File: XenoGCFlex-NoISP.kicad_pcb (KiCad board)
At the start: 2 copper layers, 23.6 x 20 mm, 21 parts, among them J1 AVR-ISP-6, U1 ATmega8A-AU

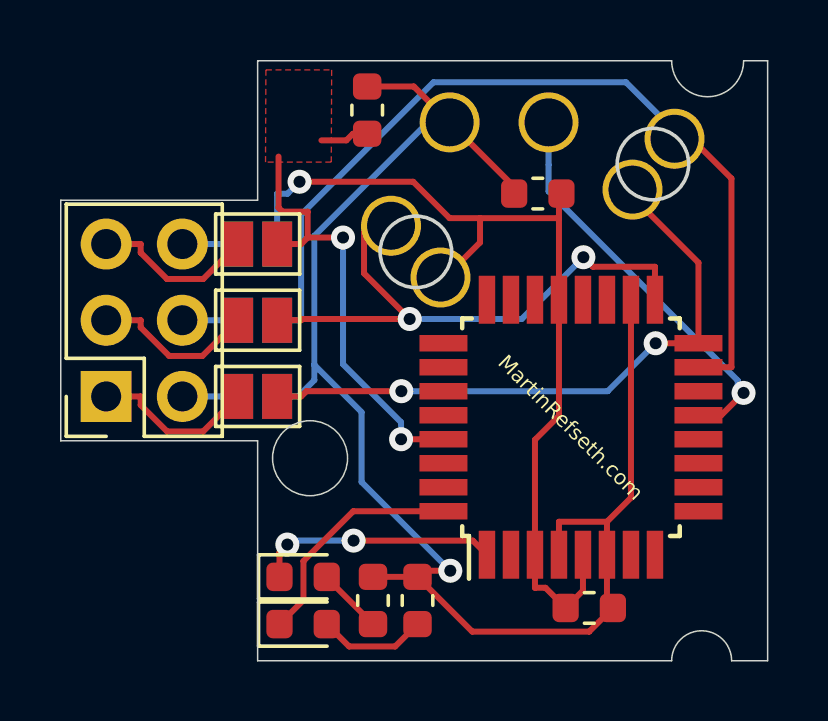
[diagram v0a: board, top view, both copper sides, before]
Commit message: Add a version without isp headers, add some stuff to the silkscreen
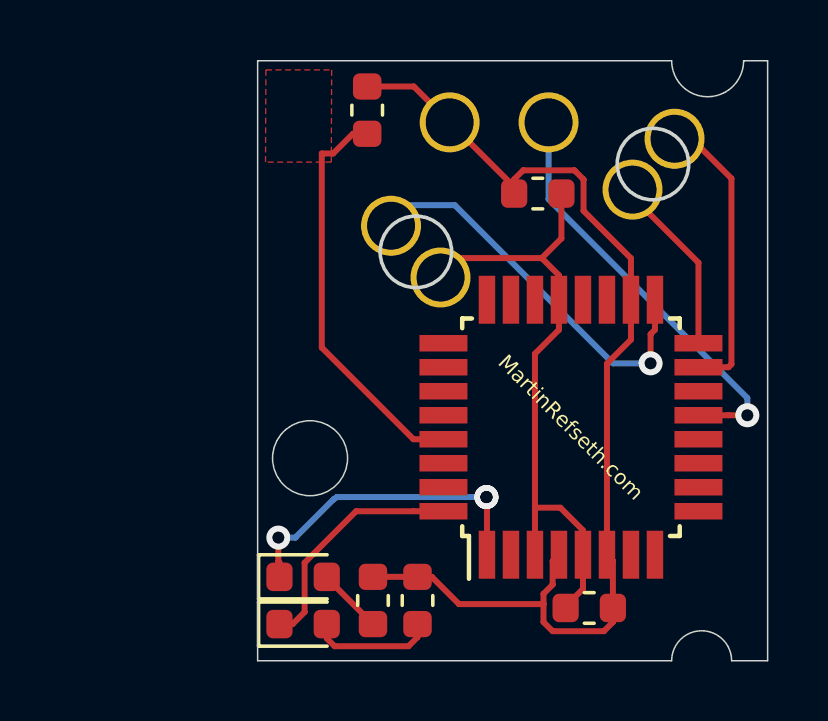
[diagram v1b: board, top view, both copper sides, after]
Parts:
- removed J1: AVR-ISP-6, Connector_PinSocket_2.54mm:PinSocket_2x03_P2.54mm_Vertical
- removed JP1, JP2, JP3, JP4, JP5, JP6: Jumper, Jumper:SolderJumper-2_P1.3mm_Open_Pad1.0x1.5mm
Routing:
- net MOSI: track 27.9 -> 9.15 mm
- net MISO: track 20.0 -> 5.23 mm, vias 2 -> 0
- net VCC: track 51.6 -> 37.5 mm, vias 1 -> 0
- net GND: track 30.2 -> 20.4 mm, vias 1 -> 0
- net SCK: track 18.9 -> 12.9 mm, vias 2 -> 1
- net Net-(J1-Pad1): track 5.53 -> 0.00 mm
- net Net-(J1-Pad5): track 5.53 -> 0.00 mm
- net Net-(J1-Pad3): track 5.52 -> 0.00 mm
- net Net-(D2-Pad1): track 8.09 -> 11.0 mm, vias 2 -> 3
- net RESET: track 16.4 -> 13.6 mm, vias 2 -> 0
- net Net-(J1-Pad6): track 1.86 -> 0.00 mm
- net Net-(J1-Pad4): track 1.86 -> 0.00 mm
- net Net-(J1-Pad2): track 1.86 -> 0.00 mm
- net PB1: track 13.5 -> 14.3 mm
- net Net-(D1-Pad2): track 3.64 -> 4.17 mm
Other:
- board size 23.6 x 20 mm -> 17 x 20 mm

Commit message: Remove text
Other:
- board text removed: "Put this side towards the board Or don't i'm a PCB not a cop."
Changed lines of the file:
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@@
   (general
     (thickness 0.24)
-    (drawings 14)
+    (drawings 13)
     (tracks 105)
     (zones 0)
@@
   (gr_line (start 155.85694 60.18022) (end 155.05684 60.18022) (layer Edge.Cuts) (width 0.05))
   (gr_line (start 152.65684 60.18022) (end 138.857 60.18022) (layer Edge.Cuts) (width 0.05))
-  (gr_text "Put this side towards the board\nOr don't i'm a PCB not a cop." (at 145.33118 79.16164) (layer B.SilkS)
-    (effects (font (size 0.5 0.5) (thickness 0.1)) (justify mirror))
-  )
   (gr_arc (start 153.65694 80.18018) (end 154.65694 80.18018) (angle -180) (layer Edge.Cuts) (width 0.05))
   (gr_arc (start 153.85684 60.18022) (end 152.65684 60.18022) (angle -180) (layer Edge.Cuts) (width 0.05))
